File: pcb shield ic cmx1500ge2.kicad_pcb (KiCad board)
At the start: 2 copper layers, 68.6 x 53.3 mm, 14 parts, among them J1 SMA, J2 SMA, P1 Power, P2 Analog, P3 Digital, P4 Digital, P5 CONN_01X01, P6 CONN_01X01, P7 CONN_01X01, P8 CONN_01X01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

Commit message: routing PCB sudah selesai
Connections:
- LM2596_1 pad 1: /+2V -> +5V
- LM2596_1 pad 3: +5V -> /+2V
- U1 pad 41: Net-(U1-Pad41) -> GND
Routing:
- net Net-(J1-Pad1): track 12.0 -> 43.2 mm, vias 0 -> 1
- net Net-(J2-Pad1): track 7.14 -> 28.6 mm
- net /3(**): track 0.00 -> 19.5 mm, vias 0 -> 1
- net Net-(J2-Pad2): track 17.5 -> 35.8 mm, vias 0 -> 1
- net Net-(TXS0108E-8_1-Pad3): track 6.71 -> 21.8 mm
- net /4: track 0.00 -> 14.3 mm
- net Net-(TXS0108E-8_1-Pad2): track 1.89 -> 15.4 mm
- net GND: track 168.9 -> 179.0 mm
- net Net-(J1-Pad2): track 0.00 -> 5.49 mm
- net +5V: track 54.8 -> 59.0 mm
- net /+2V: track 41.0 -> 42.5 mm
- added copper zone on B.Cu, net GND
- added copper zone on F.Cu, net GND

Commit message: penambahan komponen 3d
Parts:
- renumbered J1 to GNSS, J2 to LPWA
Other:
- board text added: "debag"
- board text added: "prog"

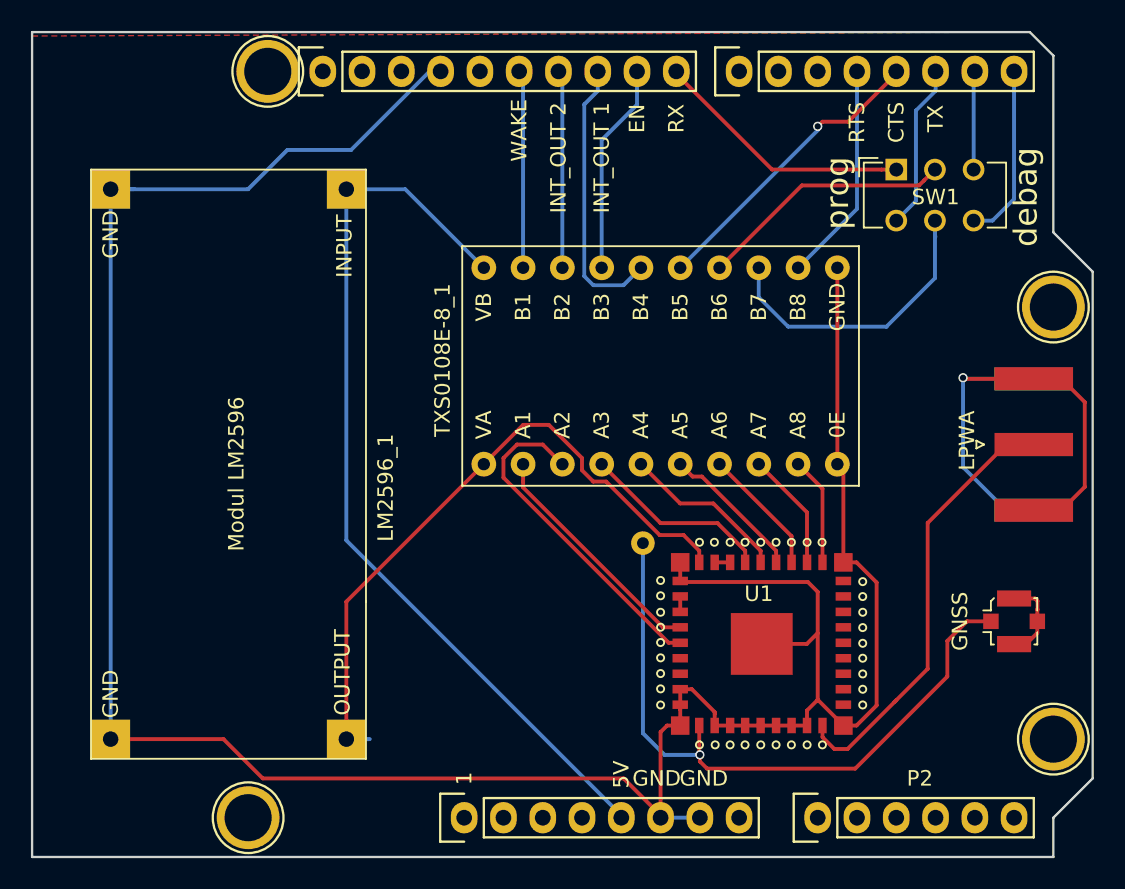
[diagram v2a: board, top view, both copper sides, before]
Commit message: penambahan via untuk grounding
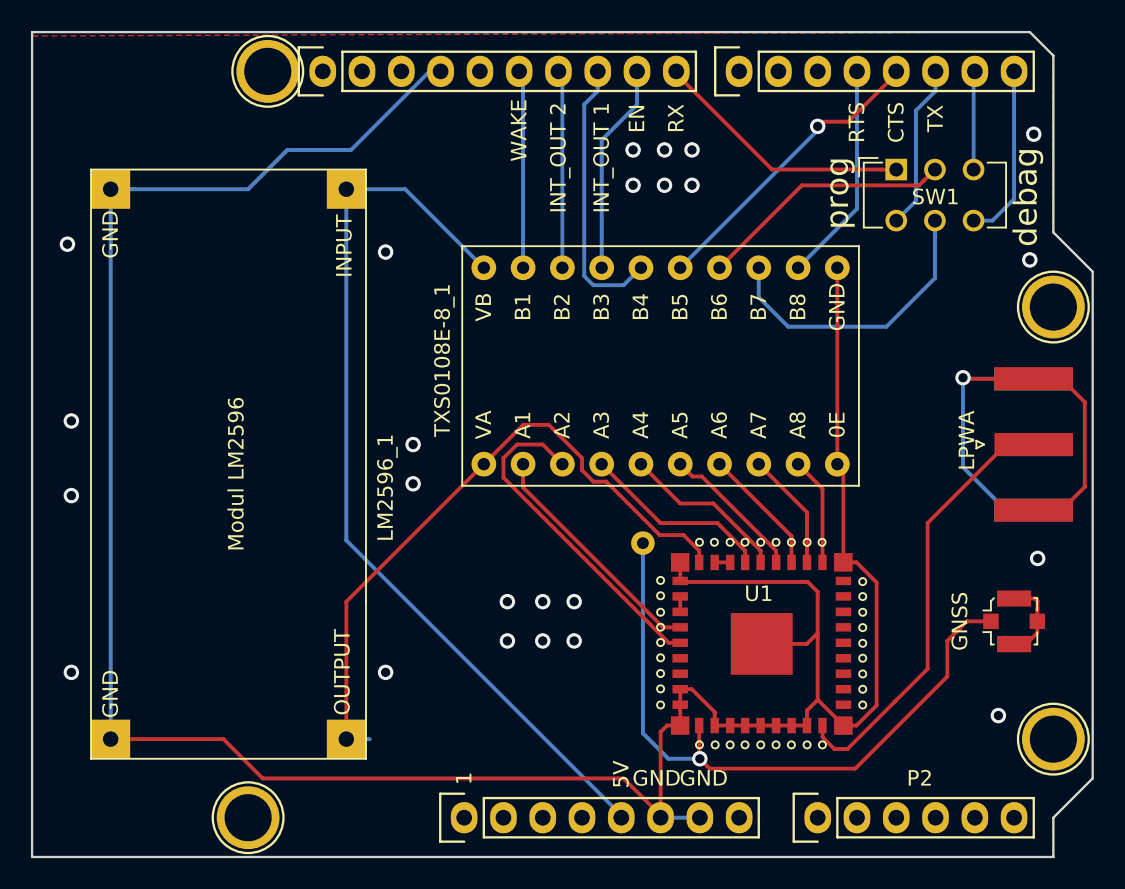
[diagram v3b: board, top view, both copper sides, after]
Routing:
- net GND: vias 0 -> 1
- net (no net): vias 0 -> 23
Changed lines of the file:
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@@
     (thickness 1.6)
     (drawings 21)
-    (tracks 184)
+    (tracks 208)
     (zones 0)
     (modules 14)
@@
   (gr_line (start 178.435 94.615) (end 178.435 102.235) (angle 90) (layer Dwgs.User) (width 0.15))
   (gr_line (start 173.355 94.615) (end 178.435 94.615) (angle 90) (layer Dwgs.User) (width 0.15))
+  (via (at 175.514 87.757) (size 1) (drill 0.6) (layers F.Cu B.Cu) (net 0))
+  (via (at 176.022 107.061) (size 1) (drill 0.6) (layers F.Cu B.Cu) (net 0))
+  (via (at 173.482 117.221) (size 1) (drill 0.6) (layers F.Cu B.Cu) (net 0))
+  (via (at 146.05 109.855) (size 1) (drill 0.6) (layers F.Cu B.Cu) (net 0))
+  (via (at 149.86 80.645) (size 1) (drill 0.6) (layers F.Cu B.Cu) (net 0))
+  (via (at 144.018 109.855) (size 1) (drill 0.6) (layers F.Cu B.Cu) (net 0))
+  (via (at 141.732 109.855) (size 1) (drill 0.6) (layers F.Cu B.Cu) (net 0))
+  (via (at 144.018 112.395) (size 1) (drill 0.6) (layers F.Cu B.Cu) (net 0))
+  (via (at 146.05 112.395) (size 1) (drill 0.6) (layers F.Cu B.Cu) (net 0))
+  (via (at 141.732 112.395) (size 1) (drill 0.6) (layers F.Cu B.Cu) (net 0))
+  (via (at 151.892 80.645) (size 1) (drill 0.6) (layers F.Cu B.Cu) (net 0))
+  (via (at 153.67 80.645) (size 1) (drill 0.6) (layers F.Cu B.Cu) (net 0))
+  (via (at 151.892 82.931) (size 1) (drill 0.6) (layers F.Cu B.Cu) (net 0))
+  (via (at 153.67 82.931) (size 1) (drill 0.6) (layers F.Cu B.Cu) (net 0))
+  (via (at 149.86 82.931) (size 1) (drill 0.6) (layers F.Cu B.Cu) (net 0))
+  (via (at 133.858 87.249) (size 1) (drill 0.6) (layers F.Cu B.Cu) (net 0))
+  (via (at 113.284 86.741) (size 1) (drill 0.6) (layers F.Cu B.Cu) (net 0))
+  (via (at 135.636 99.695) (size 1) (drill 0.6) (layers F.Cu B.Cu) (net 0))
+  (via (at 135.636 102.235) (size 1) (drill 0.6) (layers F.Cu B.Cu) (net 0))
+  (via (at 133.858 114.427) (size 1) (drill 0.6) (layers F.Cu B.Cu) (net 0))
+  (via (at 113.538 114.427) (size 1) (drill 0.6) (layers F.Cu B.Cu) (net 0))
+  (via (at 113.538 98.171) (size 1) (drill 0.6) (layers F.Cu B.Cu) (net 0))
+  (via (at 113.538 102.997) (size 1) (drill 0.6) (layers F.Cu B.Cu) (net 0))
   (segment (start 131.318 83.185) (end 135.128 83.185) (width 0.25) (layer B.Cu) (net 3))
   (segment (start 135.128 83.185) (end 140.208 88.265) (width 0.25) (layer B.Cu) (net 3))
@@
   (segment (start 153.658 115.515) (end 155.138 116.995) (width 0.25) (layer F.Cu) (net 4))
   (segment (start 161.798 116.205) (end 161.808002 116.205) (width 0.25) (layer F.Cu) (net 4))
+  (via (at 175.768 79.629) (size 1) (drill 0.6) (layers F.Cu B.Cu) (net 4))
   (segment (start 147.828 88.265) (end 147.828 80.01) (width 0.25) (layer B.Cu) (net 13))
   (segment (start 150.114 77.724) (end 150.114 75.565) (width 0.25) (layer B.Cu) (net 13))
@@
   (segment (start 161.798 79.375) (end 161.798 79.121) (width 0.25) (layer B.Cu) (net 19))
   (segment (start 152.908 88.265) (end 161.798 79.375) (width 0.25) (layer B.Cu) (net 19))
-  (via (at 161.798 79.121) (size 0.6) (drill 0.4) (layers F.Cu B.Cu) (net 19))
+  (via (at 161.798 79.121) (size 1) (drill 0.6) (layers F.Cu B.Cu) (net 19))
   (segment (start 166.878 75.7174) (end 166.878 75.565) (width 0.25) (layer F.Cu) (net 19))
   (segment (start 163.774399 78.821001) (end 166.878 75.7174) (width 0.25) (layer F.Cu) (net 19))
@@
   (segment (start 142.748 75.819) (end 142.494 75.565) (width 0.25) (layer B.Cu) (net 30))
   (segment (start 142.748 88.265) (end 142.748 75.819) (width 0.25) (layer B.Cu) (net 30))
-  (segment (start 150.495 118.364) (end 150.495 106.0704) (width 0.25) (layer B.Cu) (net 31))
-  (segment (start 154.178 119.761) (end 151.892 119.761) (width 0.25) (layer B.Cu) (net 31))
-  (segment (start 151.892 119.761) (end 150.495 118.364) (width 0.25) (layer B.Cu) (net 31))
-  (via (at 154.178 119.761) (size 0.6) (drill 0.4) (layers F.Cu B.Cu) (net 31))
   (segment (start 170.18 112.395) (end 171.45 111.125) (width 0.25) (layer F.Cu) (net 31))
   (segment (start 170.18 114.693) (end 170.18 112.395) (width 0.25) (layer F.Cu) (net 31))
   (segment (start 154.138 119.721) (end 154.178 119.761) (width 0.25) (layer F.Cu) (net 31))
   (segment (start 171.45 111.125) (end 172.998 111.125) (width 0.25) (layer F.Cu) (net 31))
-  (segment (start 154.178 120.185264) (end 154.642736 120.65) (width 0.25) (layer F.Cu) (net 31))
-  (segment (start 154.178 119.761) (end 154.178 120.185264) (width 0.25) (layer F.Cu) (net 31))
-  (segment (start 154.642736 120.65) (end 164.223 120.65) (width 0.25) (layer F.Cu) (net 31))
   (segment (start 164.223 120.65) (end 170.18 114.693) (width 0.25) (layer F.Cu) (net 31))
-  (segment (start 154.138 117.865) (end 154.138 119.721) (width 0.25) (layer F.Cu) (net 31))
+  (via (at 154.178 120.015) (size 1) (drill 0.6) (layers F.Cu B.Cu) (net 31))
+  (segment (start 154.813 120.65) (end 154.178 120.015) (width 0.25) (layer F.Cu) (net 31))
+  (segment (start 164.223 120.65) (end 154.813 120.65) (width 0.25) (layer F.Cu) (net 31))
+  (segment (start 152.146 120.015) (end 154.178 120.015) (width 0.25) (layer B.Cu) (net 31))
+  (segment (start 150.495 106.0704) (end 150.495 118.364) (width 0.25) (layer B.Cu) (net 31))
+  (segment (start 150.495 118.364) (end 152.146 120.015) (width 0.25) (layer B.Cu) (net 31))
+  (segment (start 154.138 119.975) (end 154.178 120.015) (width 0.25) (layer F.Cu) (net 31))
+  (segment (start 154.138 117.865) (end 154.138 119.975) (width 0.25) (layer F.Cu) (net 31))
   (segment (start 175.224 112.649) (end 175.998 111.875) (width 0.25) (layer F.Cu) (net 32))
   (segment (start 175.122 112.649) (end 175.224 112.649) (width 0.25) (layer F.Cu) (net 32))
@@
   (segment (start 171.196 101.163) (end 173.978 103.945) (width 0.25) (layer B.Cu) (net 34))
   (segment (start 171.196 95.377) (end 171.196 101.163) (width 0.25) (layer B.Cu) (net 34))
-  (via (at 171.196 95.377) (size 0.6) (drill 0.4) (layers F.Cu B.Cu) (net 34))
+  (via (at 171.196 95.377) (size 1) (drill 0.6) (layers F.Cu B.Cu) (net 34))
   (segment (start 175.768 95.445) (end 177.558 95.445) (width 0.25) (layer F.Cu) (net 34))
   (segment (start 175.768 95.445) (end 171.264 95.445) (width 0.25) (layer F.Cu) (net 34))
